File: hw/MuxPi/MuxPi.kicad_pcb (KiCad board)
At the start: 2 copper layers, 138.8 x 55 mm, 418 parts, among them CON1 PC-GK2.1, IC1 AT24C02D-SSHM-T, IC2 ATTINY10-TS8R, J1 471511001 (HDMI), J2 112K-TBA0-RA1, J3 TJACKCFL8P8CSR06M1, J4 CONN_01X04, J5 CONN_01X05, K1 1-1462037-4, K2 1-1462037-4, P1 DS1021-1*6SF1-1, P10 USB_OTG_MICRO_USB, P11 ZL262-20SG, P12 ZL201-04G, P13 PBTD16S, P14 ZL262-26DG, P15 PBTD16S, P16 UBA-4R-D14-4D, P17 USBA-2G, P18 CONN_02X03, P2 XY2500V-D(5.08)-2PIN, P3 XY2500V-D(5.08)-2PIN, P4 T821108A1S100CEU, P5 NS25-W2P, P6 NS25-W2P, P7 NS25-W2P, P8 NS25-W2P, P9 T821108A1S100CEU, Q1 2N7002, Q10 2N7002, Q11 BSO130P03S, Q12 BSO130P03S, Q13 2N7002, Q14 2N7002, Q15 BSO130P03S, Q16 IRLML2246TRPBF, Q2 2N7002, Q3 2N7002, Q4 MMBT4403LT1, Q5 MMBT4403LT1, Q8 2N7002, Q9 2N7002, SW1 DTSM-62N-V-B, SW2 DTSM-62N-V-B, U1 STM32F030C6T6, U10 LD1117S33CTR, U11 93AA56AT-I/OT, U12 LAN9500A-ABZJ, U13 TS3USB30EDGSR, U14 FT230XQ, U15 MCP6002-E/SN, U2 MCP6002-E/SN, U3 OLED-AG-128032DY-Y (YELLOW), U4 ACS712ELCTR-05B-T, U5 SN74LVC2T45DCTT, U6 SN74LVC2T45DCTT, U7 MC74HC1G04DTT1G, U8 TS3A27518EPWR, U9 USB2640-HZH-02, Y1 ABM3B-8.000MHZ-10-1-U-T, Y2 LF XTAL012504 - 24MHz, Y3 25.00M-SMDHC49S

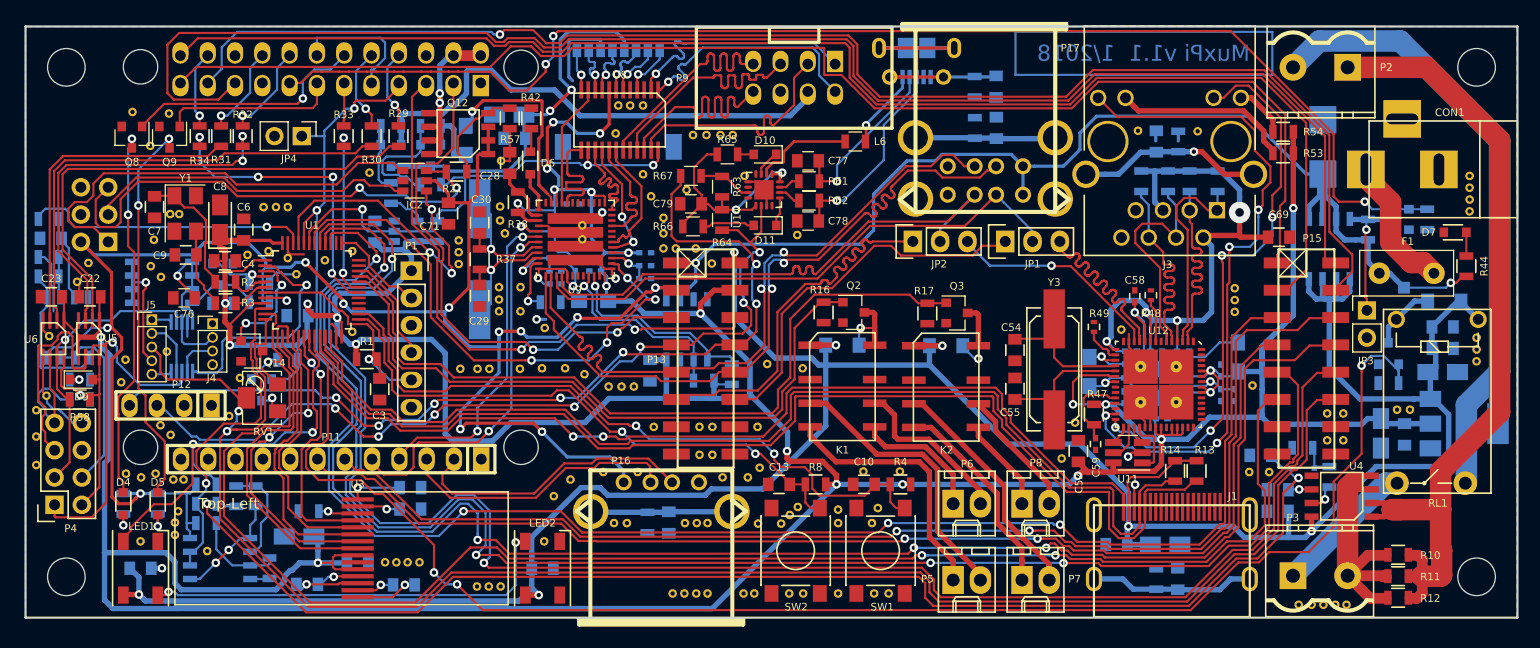
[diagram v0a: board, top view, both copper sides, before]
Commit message: Add detailed info to MuxPi electronic components
The additional information includes manufacturer names and
manufacturer symbols for all components except ceramic capacitors
and resistors. It allows to create BOM (Bill Of Materials) with
actual product names.

Change-Id: Id1c518bba60322d4b8b132ad14261806070abc27
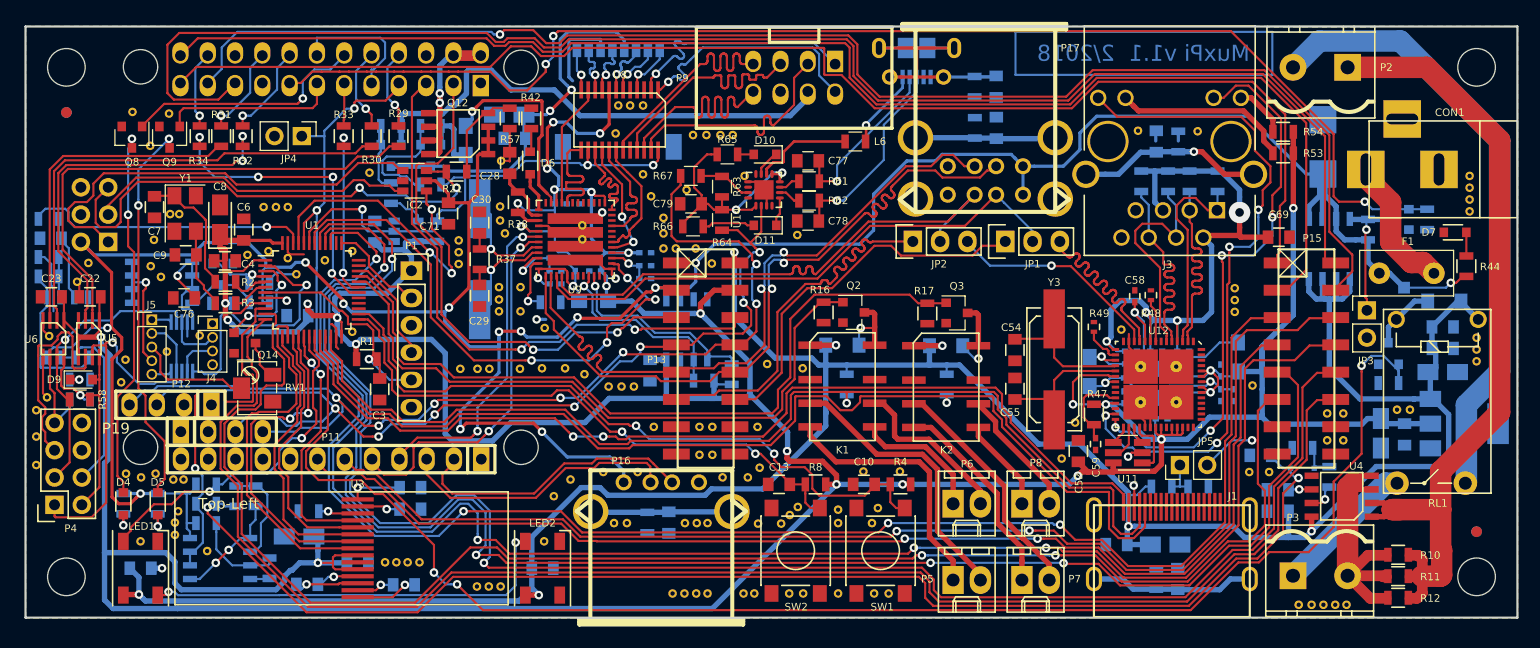
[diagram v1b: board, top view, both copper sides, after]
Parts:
- removed Q16: IRLML2246TRPBF, TO_SOT_Packages_SMD:SOT-23
- removed the V1 at (16.9, 174.3)
- removed the V1 at (34.0, 176.2)
- removed the V1 at (35.0, 172.7)
- removed the V1 at (28.5, 178.0)
- removed the V1 at (27.6, 177.1)
- added JP5: Jumper_NO_Small, Pin_Headers:Pin_Header_Straight_1x02_Pitch2.54mm, F.Cu at (122.4, 180.8)
- added P19: ZL201-04G, mux-footprints:pin_strip_2.54_s_1x4, F.Cu at (33.3, 177.7)
- added R77: 3.3K 1%, Resistors_SMD:R_0805, B.Cu at (124.1, 182.8)
- added REF**: Fiducial_1mm_Dia_2mm_Outer, Fiducials:Fiducial_1mm_Dia_2mm_Outer, B.Cu at (18.8, 148.0)
- added REF**: Fiducial_1mm_Dia_2mm_Outer, Fiducials:Fiducial_1mm_Dia_2mm_Outer, F.Cu at (150.0, 187.0)
- added REF**: Fiducial_1mm_Dia_2mm_Outer, Fiducials:Fiducial_1mm_Dia_2mm_Outer, F.Cu at (18.8, 148.0)
- added REF**: Fiducial_1mm_Dia_2mm_Outer, Fiducials:Fiducial_1mm_Dia_2mm_Outer, B.Cu at (150.0, 187.0)
- added V1: VIA_0408, mux-footprints:VIA_0408, F.Cu at (17.0, 174.5)
- added V1: VIA_0408, mux-footprints:VIA_0408, F.Cu at (31.2, 168.8)
- R13, R14: moved to B.Cu
- R26: value 10K -> 3.3K 1%
- moved R26 82.2 mm to (120.7, 182.8), turned to 0 degrees
- moved R14 31.6 mm to (91.4, 173.3)
- moved R13 24.6 mm to (100.7, 173.3)
- moved RV1 1.01 mm to (36.5, 173.7)
- moved Q14 0.99 mm to (35.4, 169.4)
- moved P12 0.05 mm to (28.5, 175.2)
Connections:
- J5 pad 3: /Lthor/ADC2 -> /Lthor/USB_ID
- P15 pad 11: /Lthor/ADC1 -> /Microcontroller/ADC1
- P15 pad 12: /Lthor/ADC2 -> /Microcontroller/ADC2
- R26 pad 1: +3V3 -> VDD
- R26 pad 2: /Lthor/ADC1 -> Net-(JP5-Pad1)
- RV1 pad 2: /Lthor/ADC2 -> /Lthor/USB_ID
- U1 pad 11: /Lthor/ADC1 -> /Microcontroller/ADC1
- U1 pad 12: /Lthor/ADC2 -> /Microcontroller/ADC2
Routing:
- net /Lthor/ADC2: track 160.7 -> 0.00 mm, vias 2 -> 0
- net /Microcontroller/ADC1: track 0.00 -> 149.2 mm, vias 0 -> 3
- net /Lthor/ADC1: track 147.3 -> 0.00 mm, vias 3 -> 0
- net /Microcontroller/ADC2: track 0.00 -> 144.0 mm
- net /Lthor/USB_ID: track 0.00 -> 10.8 mm
- net /NanoPi/PI_UART0_RX: track 86.1 -> 95.9 mm
- net /NanoPi/PI_UART0_TX: track 81.0 -> 90.5 mm
- net +3V3: track 506.2 -> 497.0 mm
- net /Microcontroller/TIM1_CH1: track 39.1 -> 32.3 mm
- net VDD: track 250.3 -> 244.9 mm
- net GND: track 80.1 -> 75.5 mm
- net Net-(P4-Pad7): track 13.2 -> 9.07 mm
- net /Hdmi/HDMI_SCL: track 104.1 -> 100.2 mm, vias 0 -> 1
- net Net-(JP5-Pad1): track 0.00 -> 3.40 mm
- net /Hdmi/HDMI_SDA: track 101.2 -> 97.9 mm, vias 0 -> 1
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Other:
- board text added: "35.40"
- board text added: "40.00"
- board text added: "?\A1;∅3.00x4"
- board text added: "AUDIO"
- board text added: "CD"
- board text added: "CD/DAT3"
- board text added: "CLK"
- board text added: "CMD"
- board text added: "DAT0"
- board text added: "DAT1"
- board text added: "DAT2"
- board text added: "G"
- board text added: "LAN1"
- board text added: "Lite"
- board text added: "MICROSD"
- board text added: "MuxPi v1.1 2/2018"
- board text added: "NanoPi NEO V1.31"
- board text added: "PWR"
- board text added: "STAT"
- board text added: "USBH1"
- board text added: "VDD"
- board text added: "VSS"
- board text removed: "MuxPi v1.1 1/2018"

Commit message: Update hardware design to version 1.2
Change-Id: I36445887bfaa5fada88d8bf3915603605de47512
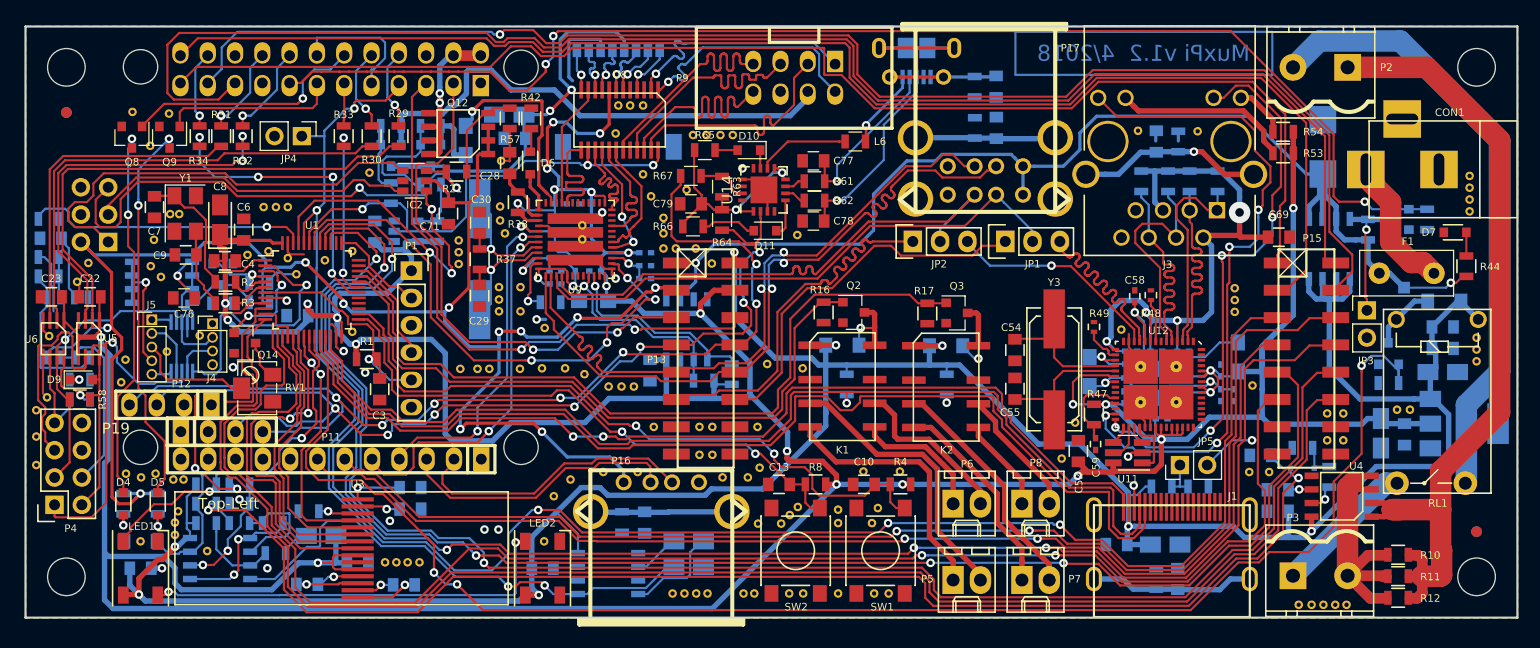
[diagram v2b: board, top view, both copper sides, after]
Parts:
- removed the V1 at (71.0, 186.2)
- removed the V1 at (69.8, 186.2)
- removed the V1 at (76.3, 186.2)
- removed the V1 at (77.5, 186.2)
- removed the V1 at (78.5, 186.2)
- removed the V1 at (57.0, 192.1)
- removed the V1 at (58.1, 192.1)
- removed the V1 at (59.2, 192.1)
- removed the V1 at (81.9, 153.9)
- added C81: 10uF/10V, Capacitors_Tantalum_SMD:CP_Tantalum_Case-A_EIA-3216-18_Reflow, B.Cu at (76.7, 187.9)
- added C82: 10uF/10V, Capacitors_Tantalum_SMD:CP_Tantalum_Case-A_EIA-3216-18_Reflow, B.Cu at (76.7, 190.3)
- added D13: STPS1L30A, mux-footprints:Sub_SMA, B.Cu at (25.7, 187.9)
- added R78: 1K 1%, Resistors_SMD:R_0805, B.Cu at (34.9, 184.4)
- added R79: 1K 1%, Resistors_SMD:R_0805, B.Cu at (34.9, 182.6)
- added U16: ICL7660, mux-footprints:SOIC-8, B.Cu at (69.2, 190.9)
- U14: footprint Housings_DFN_QFN:QFN-16-1EP_3x3mm_Pitch0.5mm -> Housings_DFN_QFN:QFN-16-1EP_4x4mm_Pitch0.65mm
- moved R74 2.97 mm to (38.0, 186.2), turned to 180 degrees
- moved R70 2.52 mm to (34.9, 186.2), turned to 180 degrees
- moved R35 2.35 mm to (70.5, 186.1)
- moved C27 2.25 mm to (72.6, 186.2)
- moved R65 2.14 mm to (78.2, 151.5)
- moved C75 2.05 mm to (42.5, 187.4)
- moved D10 1.55 mm to (82.3, 151.5)
- moved R72 1.50 mm to (38.2, 189.0), turned to 0 degrees
- moved C77 0.50 mm to (88.3, 152.5)
- moved C78 0.50 mm to (88.3, 158.1)
- moved D11 0.50 mm to (83.8, 159.0)
- moved R61 0.50 mm to (88.4, 154.4)
- moved R62 0.50 mm to (88.4, 156.2)
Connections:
- R18 pad 2: /Microcontroller/SOCKET_SEL -> Net-(R18-Pad2)
- R59 pad 1: +5V -> VDD
- R71 pad 1: +5V -> VDD
- R75 pad 2: /Microcontroller/SOCKET_SEL -> Net-(R18-Pad2)
- R76 pad 2: Net-(R76-Pad2) -> /Microcontroller/SOCKET_SEL
- U15 pad 4: GND -> /DUT Power Control/-VDD
- U15 pad 6: /DUT Power Control/DUT_PWR_CURRENT -> Net-(R78-Pad2)
- U15 pad 8: +5V -> VDD
- U7 pad 4: Net-(R76-Pad2) -> Net-(R18-Pad2)
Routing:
- net /DUT Power Control/-VDD: track 0.00 -> 46.8 mm, vias 0 -> 2
- net VDD: track 244.9 -> 263.6 mm, vias 7 -> 8
- net Net-(R78-Pad2): track 0.00 -> 11.1 mm, vias 0 -> 2
- net Net-(C81-Pad2): track 0.00 -> 9.32 mm
- net +5V: track 293.1 -> 283.9 mm
- net /DUT Power Control/DUT_PWR_CURRENT: track 34.5 -> 42.4 mm, vias 1 -> 2
- net /Microcontroller/ST_GPIO_2: track 151.9 -> 145.8 mm
- net Net-(R18-Pad2): track 0.00 -> 5.55 mm
- net /Microcontroller/ST_GPIO_3: track 154.6 -> 149.1 mm
- net Net-(C81-Pad1): track 0.00 -> 4.30 mm
- net Net-(R76-Pad2): track 3.70 -> 0.00 mm
- net /Microcontroller/ST_GPIO_1: track 150.8 -> 147.2 mm
- net /Microcontroller/PI_GPIO_1: track 163.5 -> 166.9 mm
- net Net-(R74-Pad1): track 10.4 -> 12.7 mm
- net Net-(C80-Pad2): track 122.9 -> 125.2 mm
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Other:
- board text added: "MuxPi v1.2 4/2018"
- board text removed: "MuxPi v1.1 2/2018"

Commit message: Update hardware design to version 1.3
Change-Id: I17b3f32943a6fd048f05d1b0d8676607dc54b976
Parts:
- removed C80: 100nF/50V, Capacitors_SMD:C_0805
- removed R68: 2K 1%, Resistors_SMD:R_0805
- removed R69: 10K 1%, Resistors_SMD:R_0805
- removed R73: 0R, Resistors_SMD:R_0805
- removed the V1 at (48.5, 189.8)
- added RV2: POT, mux-footprints:Potentiometer_Trimmer_Bourns_3214J, B.Cu at (40.2, 185.0)
- C58, C59: footprint Capacitors_SMD:C_0402 -> Capacitors_SMD:C_0805
- D12: value 1N4448WS -> BAR43CFILM; footprint Diodes_SMD:D_SOD-323F -> TO_SOT_Packages_SMD:SOT-23; moved to F.Cu
- L1, L2, L3, L4, L5: footprint Resistors_SMD:R_0805_HandSoldering -> Resistors_SMD:R_0805
- R15, R43, R56: value 330R -> 10K
- R42: value 330R -> 560R
- R48, R49: footprint Resistors_SMD:R_0402 -> Resistors_SMD:R_0805
- R70: value 1K 1% -> 10K 1%
- R71: value 100K -> 30K 1%
- R72: value 100K -> 8.2K 1%
- R74: value 3.3K 1% -> 10K 1%
- R79: value 1K 1% -> 3.3K 1%
- moved D12 51.1 mm to (91.9, 151.9), turned to 180 degrees
- moved C15 4.70 mm to (45.9, 191.7)
- moved R5 4.36 mm to (45.1, 187.3), turned to 270 degrees
- moved C58 3.09 mm to (116.9, 162.3), turned to 180 degrees
- moved C75 2.87 mm to (42.0, 190.2), turned to 90 degrees
- moved L6 2.68 mm to (94.6, 151.9), turned to 270 degrees
- moved R74 2.61 mm to (38.2, 188.8)
- moved R72 1.40 mm to (38.2, 190.4)
- moved R48 1.14 mm to (119.4, 163.9)
- moved C59 0.65 mm to (114.5, 179.5)
- moved R49 0.45 mm to (114.4, 167.5)
- turned R78 to 180 degrees
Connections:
- D12 pad 1: Net-(C80-Pad2) -> +5V
- L6 pad 2: Net-(L6-Pad2) -> Net-(D12-Pad2)
- R70 pad 2: Net-(C80-Pad2) -> Net-(R70-Pad2)
- R72 pad 2: GND -> Net-(R72-Pad2)
- R78 pad 1: GND -> Net-(R74-Pad1)
- U14 pad 10: Net-(L6-Pad2) -> Net-(D12-Pad3)
- U15 pad 5: Net-(R74-Pad1) -> GND
- U4 pad 7: Net-(R68-Pad2) -> Net-(R70-Pad2)
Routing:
- net Net-(C80-Pad2): track 125.2 -> 0.00 mm, vias 2 -> 0
- net Net-(R70-Pad2): track 0.00 -> 120.5 mm, vias 0 -> 1
- net Net-(L6-Pad2): track 8.61 -> 0.00 mm
- net Net-(D12-Pad3): track 0.00 -> 8.27 mm
- net Net-(R72-Pad2): track 0.00 -> 7.16 mm
- net Net-(R70-Pad1): track 10.6 -> 5.61 mm
- net Net-(R74-Pad1): track 12.7 -> 8.24 mm, vias 2 -> 0
- net Net-(C58-Pad1): track 10.4 -> 14.2 mm
- net Net-(L6-Pad1): track 7.43 -> 11.1 mm
- net +5V: track 283.9 -> 287.1 mm, vias 14 -> 15
- net Net-(R68-Pad2): track 3.06 -> 0.00 mm, vias 1 -> 0
- net /DUT Power Control/-VDD: track 46.8 -> 44.7 mm
- net Net-(C15-Pad2): track 5.74 -> 3.60 mm
- net +3V3: track 496.5 -> 494.9 mm
- net /SDMux/SD_PWR_TS: track 6.94 -> 5.98 mm
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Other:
- board text added: "MuxPi v1.3 8/2018"
- board text removed: "35.40"
- board text removed: "40.00"
- board text removed: "?\A1;∅3.00x4"
- board text removed: "AUDIO"
- board text removed: "CD"
- board text removed: "CD/DAT3"
- board text removed: "CLK"
- board text removed: "CMD"
- board text removed: "DAT0"
- board text removed: "DAT1"
- board text removed: "DAT2"
- board text removed: "G"
- board text removed: "LAN1"
- board text removed: "Lite"
- board text removed: "MICROSD"
- board text removed: "MuxPi v1.2 4/2018"
- board text removed: "NanoPi NEO V1.31"
- board text removed: "PWR"
- board text removed: "STAT"
- board text removed: "USBH1"
- board text removed: "VDD"
- board text removed: "VSS"

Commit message: Silkscreen symbols update
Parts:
- P14, P18: moved to F.Cu
- moved P18 2.54 mm to (20.1, 160.0)
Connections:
- J1 pad 1: Net-(J1-Pad1) -> (no net)
- J1 pad 10: Net-(J1-Pad10) -> (no net)
- J1 pad 11: Net-(J1-Pad11) -> (no net)
- J1 pad 12: Net-(J1-Pad12) -> (no net)
- J1 pad 13: Net-(J1-Pad13) -> (no net)
- J1 pad 14: Net-(J1-Pad14) -> (no net)
- J1 pad 2: Net-(J1-Pad2) -> (no net)
- J1 pad 3: Net-(J1-Pad3) -> (no net)
- J1 pad 4: Net-(J1-Pad4) -> (no net)
- J1 pad 5: Net-(J1-Pad5) -> (no net)
- J1 pad 6: Net-(J1-Pad6) -> (no net)
- J1 pad 7: Net-(J1-Pad7) -> (no net)
- J1 pad 8: Net-(J1-Pad8) -> (no net)
- J1 pad 9: Net-(J1-Pad9) -> (no net)
- J4 pad 1: Net-(J4-Pad1) -> (no net)
- K1 pad 2: Net-(K1-Pad2) -> (no net)
- K1 pad 7: Net-(K1-Pad7) -> (no net)
- K2 pad 2: Net-(K2-Pad2) -> (no net)
- K2 pad 7: Net-(K2-Pad7) -> (no net)
- LED2 pad 2: Net-(LED2-Pad2) -> (no net)
- P1 pad 6: Net-(P1-Pad6) -> (no net)
- P10 pad 4: Net-(P10-Pad4) -> (no net)
- P11 pad 1: Net-(P11-Pad1) -> (no net)
- P11 pad 10: Net-(P11-Pad10) -> (no net)
- P11 pad 11: Net-(P11-Pad11) -> (no net)
- P11 pad 8: Net-(P11-Pad8) -> (no net)
- P11 pad 9: Net-(P11-Pad9) -> (no net)
- P12 pad 2: Net-(P12-Pad2) -> (no net)
- P13 pad 16: Net-(P13-Pad16) -> (no net)
- P14 pad 1: Net-(P14-Pad1) -> /NanoPi/PI_PWR
- P14 pad 10: /NanoPi/PI_UART1_RX -> GND
- P14 pad 11: /NanoPi/PI_UART2_TX -> /NanoPi/STATUS_LED1
- P14 pad 12: /NanoPi/STATUS_LED1 -> /NanoPi/PI_UART2_TX
- P14 pad 13: /NanoPi/STATUS_LED2 -> GND
- P14 pad 14: GND -> /NanoPi/STATUS_LED2
- P14 pad 15: /NanoPi/PWR_CTRL -> /NanoPi/PI_UART1_RTS
- P14 pad 16: /NanoPi/PI_UART1_RTS -> /NanoPi/PWR_CTRL
- P14 pad 17: Net-(P14-Pad17) -> /NanoPi/PI_UART1_CTS
- P14 pad 18: /NanoPi/PI_UART1_CTS -> (no net)
- P14 pad 19: /NanoPi/SPI0_MOSI -> GND
- P14 pad 2: /NanoPi/PI_PWR -> (no net)
- P14 pad 20: GND -> /NanoPi/SPI0_MOSI
- P14 pad 21: /NanoPi/SPI0_MISO -> /NanoPi/PI_UART2_RX
- P14 pad 22: /NanoPi/PI_UART2_RX -> /NanoPi/SPI0_MISO
- P14 pad 23: /NanoPi/SPI0_CLK -> /NanoPi/SPI0_CS
- P14 pad 24: /NanoPi/SPI0_CS -> /NanoPi/SPI0_CLK
- P14 pad 3: /NanoPi/I2C0_SDA -> /NanoPi/PI_PWR
- P14 pad 4: /NanoPi/PI_PWR -> /NanoPi/I2C0_SDA
- P14 pad 5: /NanoPi/I2C0_SCL -> GND
- P14 pad 6: GND -> /NanoPi/I2C0_SCL
- P14 pad 7: /Microcontroller/PI_GPIO_1 -> /NanoPi/PI_UART1_TX
- P14 pad 8: /NanoPi/PI_UART1_TX -> /Microcontroller/PI_GPIO_1
- P14 pad 9: GND -> /NanoPi/PI_UART1_RX
- P18 pad 1: /NanoPi/TPI_DATA -> +5V
- P18 pad 2: +5V -> /NanoPi/TPI_DATA
- P18 pad 3: /NanoPi/TPI_CLK -> (no net)
- P18 pad 4: Net-(P18-Pad4) -> /NanoPi/TPI_CLK
- P18 pad 5: /NanoPi/TPI_RST -> GND
- P18 pad 6: GND -> /NanoPi/TPI_RST
- P19 pad 2: Net-(P19-Pad2) -> (no net)
- P4 pad 6: Net-(P4-Pad6) -> (no net)
- RV1 pad 1: Net-(RV1-Pad1) -> (no net)
- RV2 pad 1: Net-(RV2-Pad1) -> (no net)
- U1 pad 27: Net-(U1-Pad27) -> (no net)
- U1 pad 28: Net-(U1-Pad28) -> (no net)
- U1 pad 29: Net-(U1-Pad29) -> (no net)
- U1 pad 35: Net-(U1-Pad35) -> (no net)
- U1 pad 36: Net-(U1-Pad36) -> (no net)
- U1 pad 38: Net-(U1-Pad38) -> (no net)
- U12 pad 1: Net-(U12-Pad1) -> (no net)
- U12 pad 14: Net-(U12-Pad14) -> (no net)
- U12 pad 22: Net-(U12-Pad22) -> (no net)
- U12 pad 23: Net-(U12-Pad23) -> (no net)
- U12 pad 26: Net-(U12-Pad26) -> (no net)
- U12 pad 37: Net-(U12-Pad37) -> (no net)
- U12 pad 41: Net-(U12-Pad41) -> (no net)
- U12 pad 42: Net-(U12-Pad42) -> (no net)
- U12 pad 43: Net-(U12-Pad43) -> (no net)
- U12 pad 44: Net-(U12-Pad44) -> (no net)
- U12 pad 45: Net-(U12-Pad45) -> (no net)
- U12 pad 46: Net-(U12-Pad46) -> (no net)
- U12 pad 47: Net-(U12-Pad47) -> (no net)
- U12 pad 53: Net-(U12-Pad53) -> (no net)
- U12 pad 54: Net-(U12-Pad54) -> (no net)
- U12 pad 55: Net-(U12-Pad55) -> (no net)
- U12 pad 56: Net-(U12-Pad56) -> (no net)
- U12 pad 7: Net-(U12-Pad7) -> (no net)
- U14 pad 12: Net-(U14-Pad12) -> (no net)
- U14 pad 14: Net-(U14-Pad14) -> (no net)
- U14 pad 16: Net-(U14-Pad16) -> (no net)
- U14 pad 4: Net-(U14-Pad4) -> (no net)
- U16 pad 1: Net-(U16-Pad1) -> (no net)
- U16 pad 6: Net-(U16-Pad6) -> (no net)
- U16 pad 7: Net-(U16-Pad7) -> (no net)
- U8 pad 3: Net-(U8-Pad3) -> (no net)
- U9 pad 11: Net-(U9-Pad11) -> (no net)
- U9 pad 19: Net-(U9-Pad19) -> (no net)
- U9 pad 20: Net-(U9-Pad20) -> (no net)
- U9 pad 22: Net-(U9-Pad22) -> (no net)
- U9 pad 23: Net-(U9-Pad23) -> (no net)
- U9 pad 26: Net-(U9-Pad26) -> (no net)
- U9 pad 27: Net-(U9-Pad27) -> (no net)
- U9 pad 28: Net-(U9-Pad28) -> (no net)
- U9 pad 29: Net-(U9-Pad29) -> (no net)
- U9 pad 30: Net-(U9-Pad30) -> (no net)
- U9 pad 31: Net-(U9-Pad31) -> (no net)
- U9 pad 36: Net-(U9-Pad36) -> (no net)
- U9 pad 6: Net-(U9-Pad6) -> (no net)
- U9 pad 7: Net-(U9-Pad7) -> (no net)
- U9 pad 8: Net-(U9-Pad8) -> (no net)
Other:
- board text added: "+3V3 SWCLK GND SWDIO NRST NC"
- board text added: "+5V +5V SDA TX USB B+ USB A+ GND GND"
- board text added: "CLK CS PI GPIO1 PI GPIO3 ST GPIO2 ADC1 GND GND"
- board text added: "VDD +3V3 SCL RX USB B- USB A- GND NC"
